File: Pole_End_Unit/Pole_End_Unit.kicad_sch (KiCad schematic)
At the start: 12 parts, among them J17 Screw_Terminal_01x01, J18 Screw_Terminal_01x01, J19 Screw_Terminal_01x01, J20 Screw_Terminal_01x01, J6 Jack-DC, U1 AMS1117-3.3

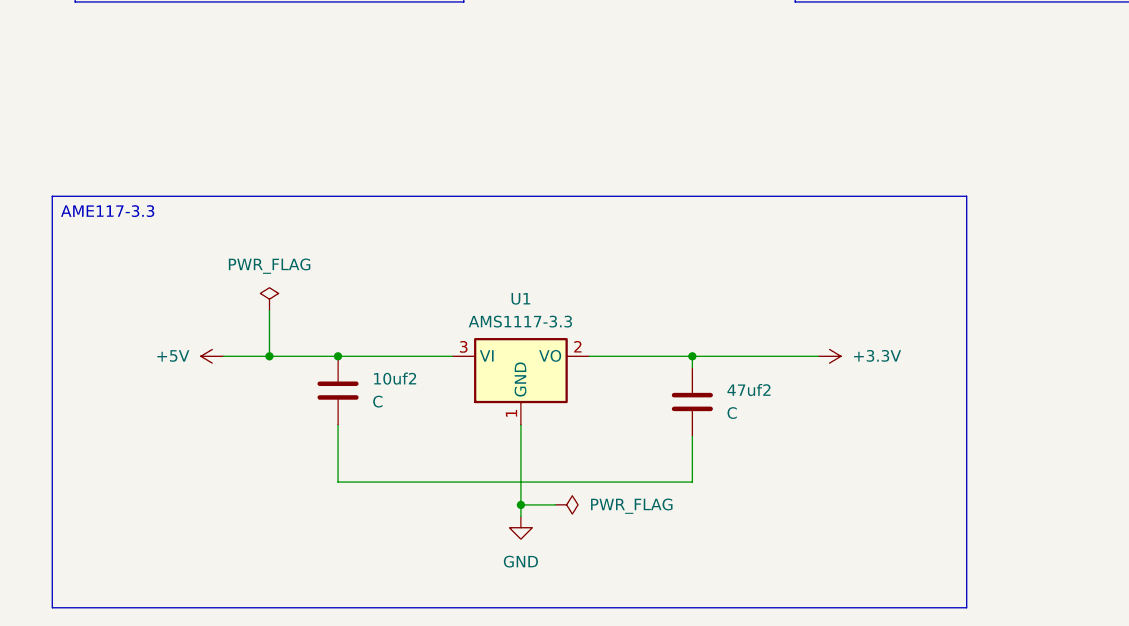
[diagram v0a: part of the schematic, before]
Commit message: Update in footprint
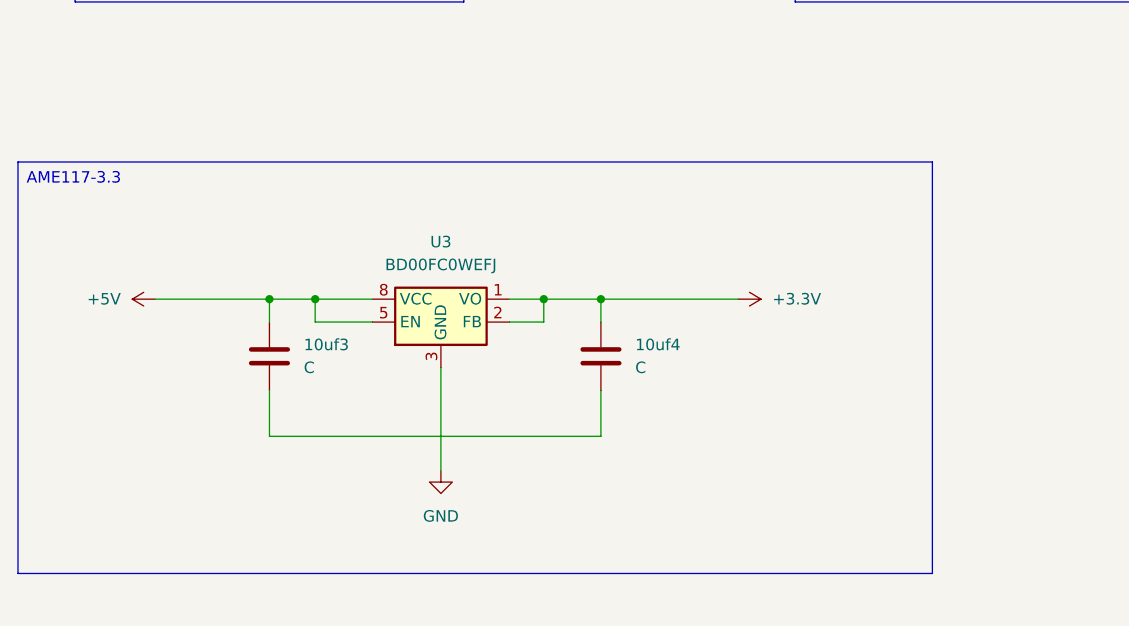
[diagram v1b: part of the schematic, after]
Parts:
- removed 10uf2, 47uf2: C, symbol Device:C
- removed U1: AMS1117-3.3, Package_TO_SOT_SMD:SOT-223-3_TabPin2, symbol Regulator_Linear:AMS1117-3.3
- added 10uf3, 10uf4: C, Capacitor_SMD:C_0603_1608Metric, symbol Device:C
- added U3: BD00FC0WEFJ, Package_SO:HTSOP-8-1EP_3.9x4.9mm_P1.27mm_EP2.4x3.2mm, symbol Regulator_Linear:BD00FC0WEFJ
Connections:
- net +3.3V: now also 10uf4.1, U3.1 (VO), U3.2 (FB)
- net +5V: now also 10uf3.1, U3.5 (EN), U3.8 (VCC)
- net GND: now also U3.3 (GND), U3.9 (GND)
- new net: 10uf3.2, 10uf4.2
